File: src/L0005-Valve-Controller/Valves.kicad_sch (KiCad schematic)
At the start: 58 parts, among them K1 AQH0223AX, K2 AQH0223AX, K3 AQH0223AX, K4 AQH0223AX, K5 AQH0223AX, K6 AQH0223AX, P10 353620650, P11 353620650, P12 353620650, P13 353620650, P3 647676-3, P4 647676-3, P5 647676-3, P6 647676-3, P7 647676-3, P8 647676-3, U3 MAX3370EXK+T, U4 MAX3370EXK+T

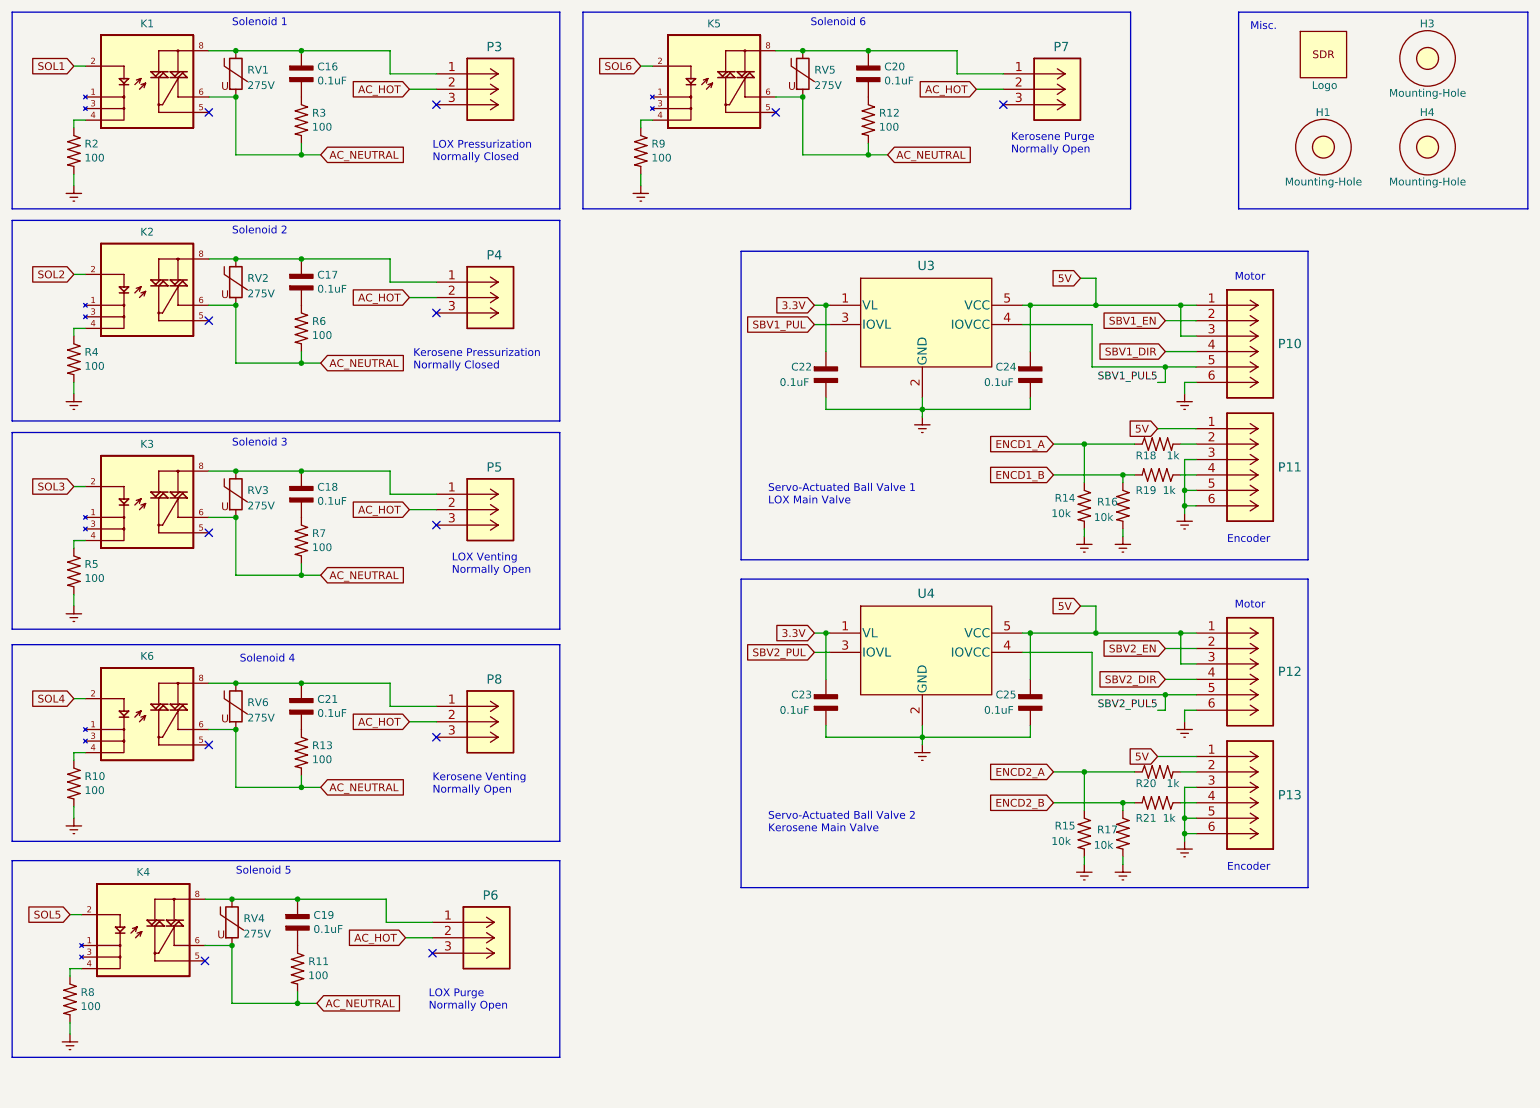
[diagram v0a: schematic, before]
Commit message: Added 5V open drain logic to stepper motor control signals
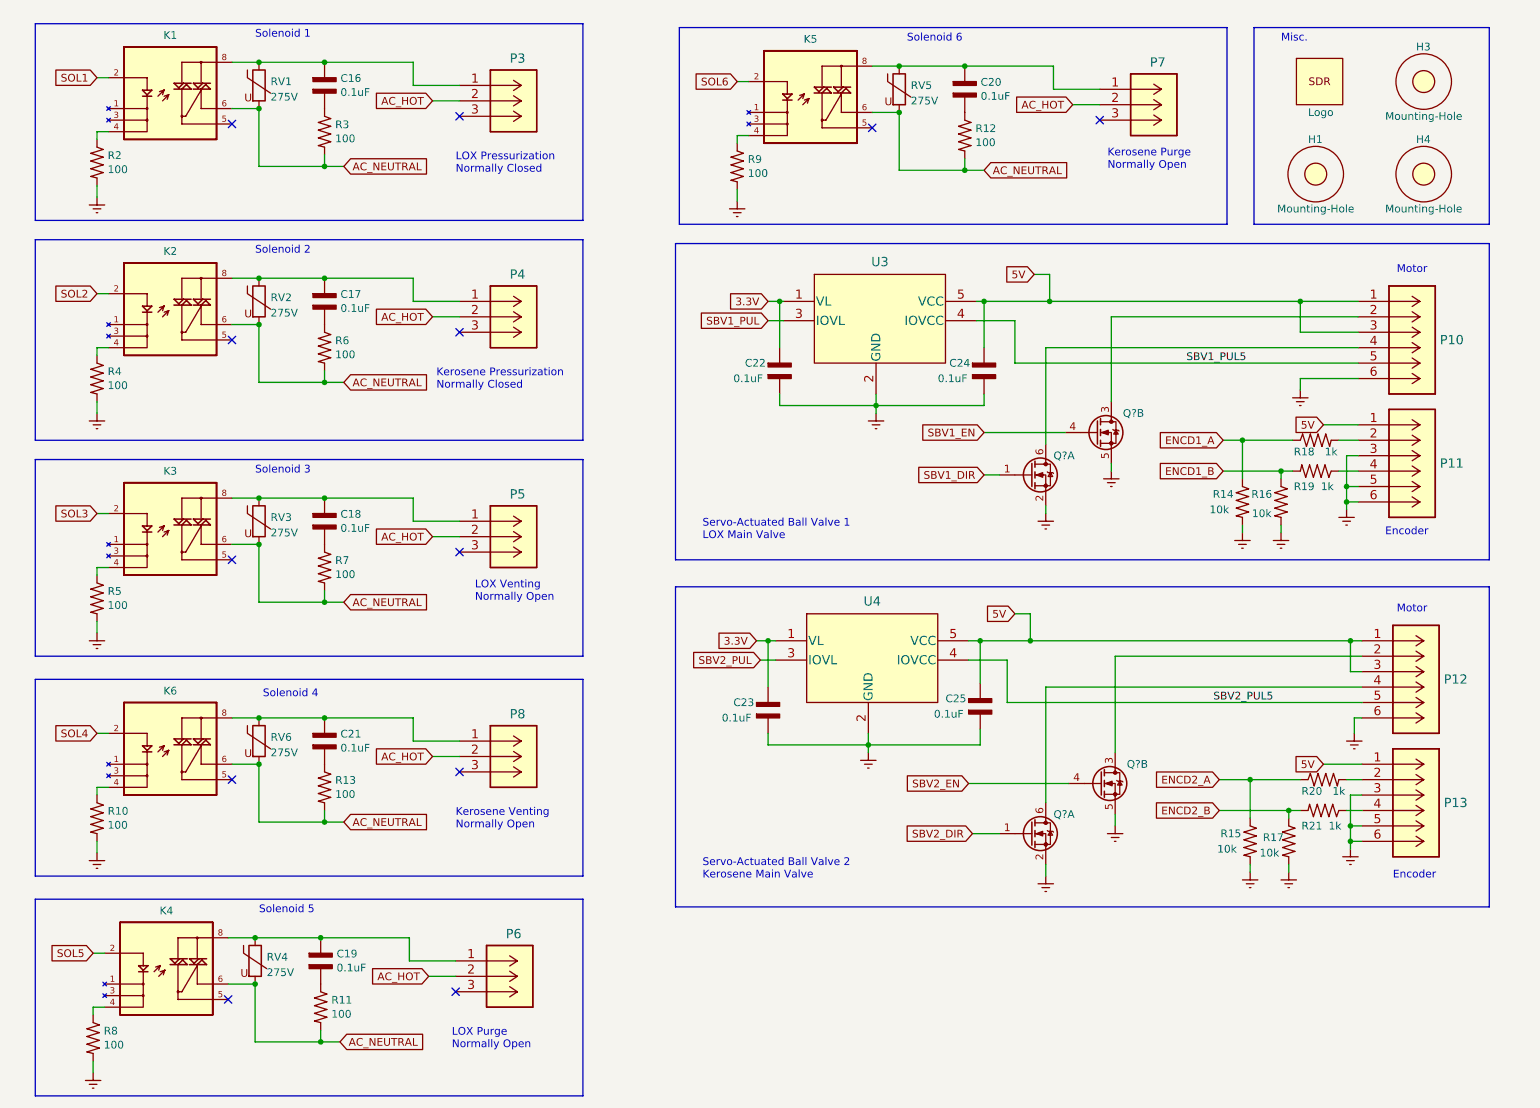
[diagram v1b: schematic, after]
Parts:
- added Q? (x4): CMLDM7003, Package_TO_SOT_THT:TO-92_Inline, symbol L0005-Valve-Controller:CMLDM7003
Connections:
- net Earth: now also Q?.2 (S), Q?.2 (S), Q?.5 (S), Q?.5 (S)
- net SBV1_DIR: now also Q?.1 (G); no longer P10.4
- net SBV1_EN: now also Q?.4 (G); no longer P10.2 (GND)
- net SBV2_DIR: now also Q?.1 (G); no longer P12.4
- net SBV2_EN: now also Q?.4 (G); no longer P12.2 (GND)
- new net: P12.4, Q?.6 (D)
- new net: P12.2 (GND), Q?.3 (D)
- new net: P10.4, Q?.6 (D)
- new net: P10.2 (GND), Q?.3 (D)
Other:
- moved on the sheet: C16, C17, C18, C19, C20, C21, C22, C23, C24, C25, H1, H3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

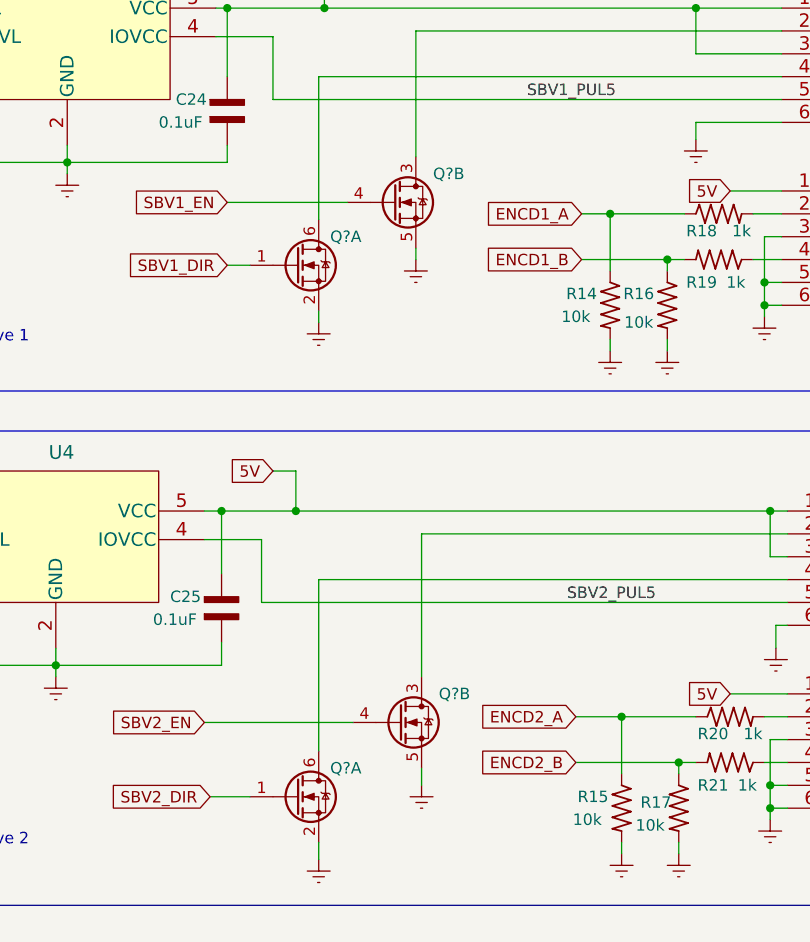
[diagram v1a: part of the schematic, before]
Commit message: Rearranged schematic
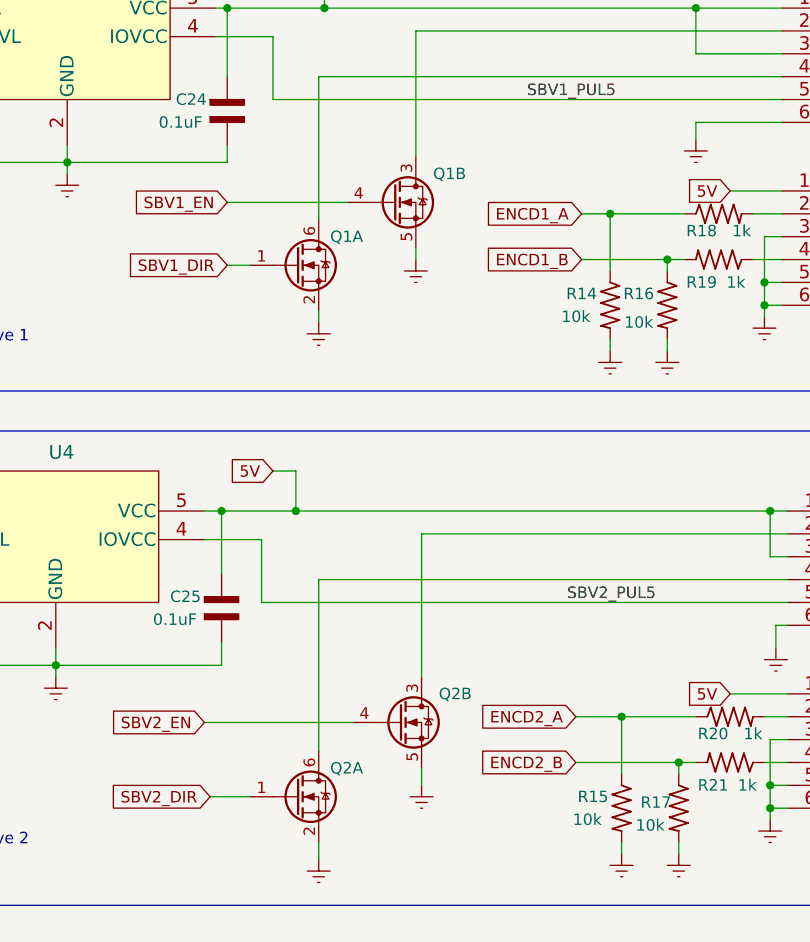
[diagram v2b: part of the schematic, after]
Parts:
- gave numbers to parts that had none: 2
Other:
- title: Solenoids -> Valves
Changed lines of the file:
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@@
   (paper "A4")
   (title_block
-    (title "Solenoids")
+    (title "Valves")
     (date "2021-12-25")
     (rev "1.0")
@@
   (symbol (lib_id "L0005-Valve-Controller:Earth") (at 186.69 95.885 0) (unit 1)
     (in_bom yes) (on_board yes)
-    (property "Reference" "#PWR?" (id 0) (at 186.69 102.235 0)
+    (property "Reference" "#PWR032" (id 0) (at 186.69 102.235 0)
       (effects (font (size 1.27 1.27)) hide)
     )
@@
   (symbol (lib_id "L0005-Valve-Controller:CMLDM7003") (at 184.15 148.59 0) (unit 1)
     (in_bom yes) (on_board yes)
-    (property "Reference" "Q?" (id 0) (at 187.96 145.415 0)
+    (property "Reference" "Q2" (id 0) (at 187.96 145.415 0)
       (effects (font (size 1.27 1.27)) (justify left))
     )
@@
   (symbol (lib_id "L0005-Valve-Controller:CMLDM7003") (at 184.15 89.535 0) (unit 1)
     (in_bom yes) (on_board yes)
-    (property "Reference" "Q?" (id 0) (at 187.96 86.36 0)
+    (property "Reference" "Q1" (id 0) (at 187.96 86.36 0)
       (effects (font (size 1.27 1.27)) (justify left))
     )
@@
   (symbol (lib_id "L0005-Valve-Controller:Earth") (at 186.69 155.575 0) (unit 1)
     (in_bom yes) (on_board yes)
-    (property "Reference" "#PWR?" (id 0) (at 186.69 161.925 0)
+    (property "Reference" "#PWR033" (id 0) (at 186.69 161.925 0)
       (effects (font (size 1.27 1.27)) hide)
     )
@@
   (symbol (lib_id "L0005-Valve-Controller:Earth") (at 197.485 88.9 0) (unit 1)
     (in_bom yes) (on_board yes)
-    (property "Reference" "#PWR?" (id 0) (at 197.485 95.25 0)
+    (property "Reference" "#PWR034" (id 0) (at 197.485 95.25 0)
       (effects (font (size 1.27 1.27)) hide)
     )
@@
   (symbol (lib_id "L0005-Valve-Controller:CMLDM7003") (at 194.945 82.55 0) (unit 2)
     (in_bom yes) (on_board yes)
-    (property "Reference" "Q?" (id 0) (at 199.39 79.375 0)
+    (property "Reference" "Q1" (id 0) (at 199.39 79.375 0)
       (effects (font (size 1.27 1.27)) (justify left))
     )
@@
   (symbol (lib_id "L0005-Valve-Controller:CMLDM7003") (at 195.58 140.335 0) (unit 2)
     (in_bom yes) (on_board yes)
-    (property "Reference" "Q?" (id 0) (at 200.025 137.16 0)
+    (property "Reference" "Q2" (id 0) (at 200.025 137.16 0)
       (effects (font (size 1.27 1.27)) (justify left))
     )
@@
   (symbol (lib_id "L0005-Valve-Controller:Earth") (at 198.12 147.32 0) (unit 1)
     (in_bom yes) (on_board yes)
-    (property "Reference" "#PWR?" (id 0) (at 198.12 153.67 0)
-      (effects (font (size 1.27 1.27)) hide)
-    )
+    (property "Reference" "#PWR035" (id 0) (at 198.12 153.67 0)
+      (effects (font (size 1.27 1.27)) hide)
+    )

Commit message: rerouted PCB to include 5V logic MOSFETS
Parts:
- Q1, Q2: footprint Package_TO_SOT_THT:TO-92_Inline -> L0005-Valve-Controller:CMLDM7003 TR
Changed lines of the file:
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@@
       (effects (font (size 1.27 1.27)) (justify left) hide)
     )
-    (property "Footprint" "Package_TO_SOT_THT:TO-92_Inline" (id 2) (at 190.246 156.464 0)
+    (property "Footprint" "L0005-Valve-Controller:CMLDM7003 TR" (id 2) (at 190.246 156.464 0)
       (effects (font (size 1.27 1.27) italic) (justify left) hide)
     )
@@
       (effects (font (size 1.27 1.27)) (justify left) hide)
     )
-    (property "Footprint" "Package_TO_SOT_THT:TO-92_Inline" (id 2) (at 190.246 97.409 0)
+    (property "Footprint" "L0005-Valve-Controller:CMLDM7003 TR" (id 2) (at 190.246 97.409 0)
       (effects (font (size 1.27 1.27) italic) (justify left) hide)
     )
@@
       (effects (font (size 1.27 1.27)) (justify left) hide)
     )
-    (property "Footprint" "Package_TO_SOT_THT:TO-92_Inline" (id 2) (at 201.041 90.424 0)
+    (property "Footprint" "L0005-Valve-Controller:CMLDM7003 TR" (id 2) (at 201.041 90.424 0)
       (effects (font (size 1.27 1.27) italic) (justify left) hide)
     )
@@
       (effects (font (size 1.27 1.27)) (justify left) hide)
     )
-    (property "Footprint" "Package_TO_SOT_THT:TO-92_Inline" (id 2) (at 201.676 148.209 0)
-      (effects (font (size 1.27 1.27) italic) (justify left) hide)
-    )
+    (property "Footprint" "L0005-Valve-Controller:CMLDM7003 TR" (id 2) (at 201.676 148.209 0)
+      (effects (font (size 1.27 1.27) italic) (justify left) hide)
+    )
